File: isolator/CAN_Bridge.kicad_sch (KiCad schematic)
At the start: 45 parts, among them J1 BOOT1, J2 BOOT0, J3 Power in, J4 JTAG5, J5 USART1, J7 HIGHVOLTAGE CAN, J8 LOWVOLTAGE CAN, SW2 SW_Push, U1 STM32F105RBTx, U2 ISO1050DUB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

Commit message: Temp changes
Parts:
- J7, J8: symbol Connector_Generic:Conn_01x02 -> Connector_Generic:Conn_01x04
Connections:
- net +12V: now also J8.2 (Pin_2); no longer J3.1 (Pin_1)
- net +5P: now also J7.2 (Pin_2)
- net GND: now also J8.1 (Pin_1); no longer J3.2 (Pin_2)
- net GND2: now also J7.1 (Pin_1)
- net HV_CANH: now also J7.3 (Pin_3); no longer J7.1 (Pin_1)
- net HV_CANL: now also J7.4 (Pin_4); no longer J7.2 (Pin_2)
- net LV_CANH: now also J8.3 (Pin_3); no longer J8.1 (Pin_1)
- net LV_CANL: now also J8.4 (Pin_4); no longer J8.2 (Pin_2)
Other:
- moved on the sheet: C16, R3, R4

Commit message: Tweaks to schematic
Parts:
- added C7: 10u, Capacitor_SMD:C_0805_2012Metric_Pad1.18x1.45mm_HandSolder, symbol Device:C_Small
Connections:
- net +5P: now also C7.1
- net GND2: now also C7.2
- net LV_RXD: no longer U1.62 (PB9), U5.1 (TXD)
- net LV_TXD: no longer U1.61 (PB8), U5.4 (RXD)
- new net MCU_CAN1_RX: U1.61 (PB8), U5.1 (TXD)
- new net MCU_CAN1_TX: U1.62 (PB9), U5.4 (RXD)
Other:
- note removed: "CAN1_RX"
- company: (none) -> SUFST - Southampton University Formula Student Team
- title: (none) -> TEM Isolator

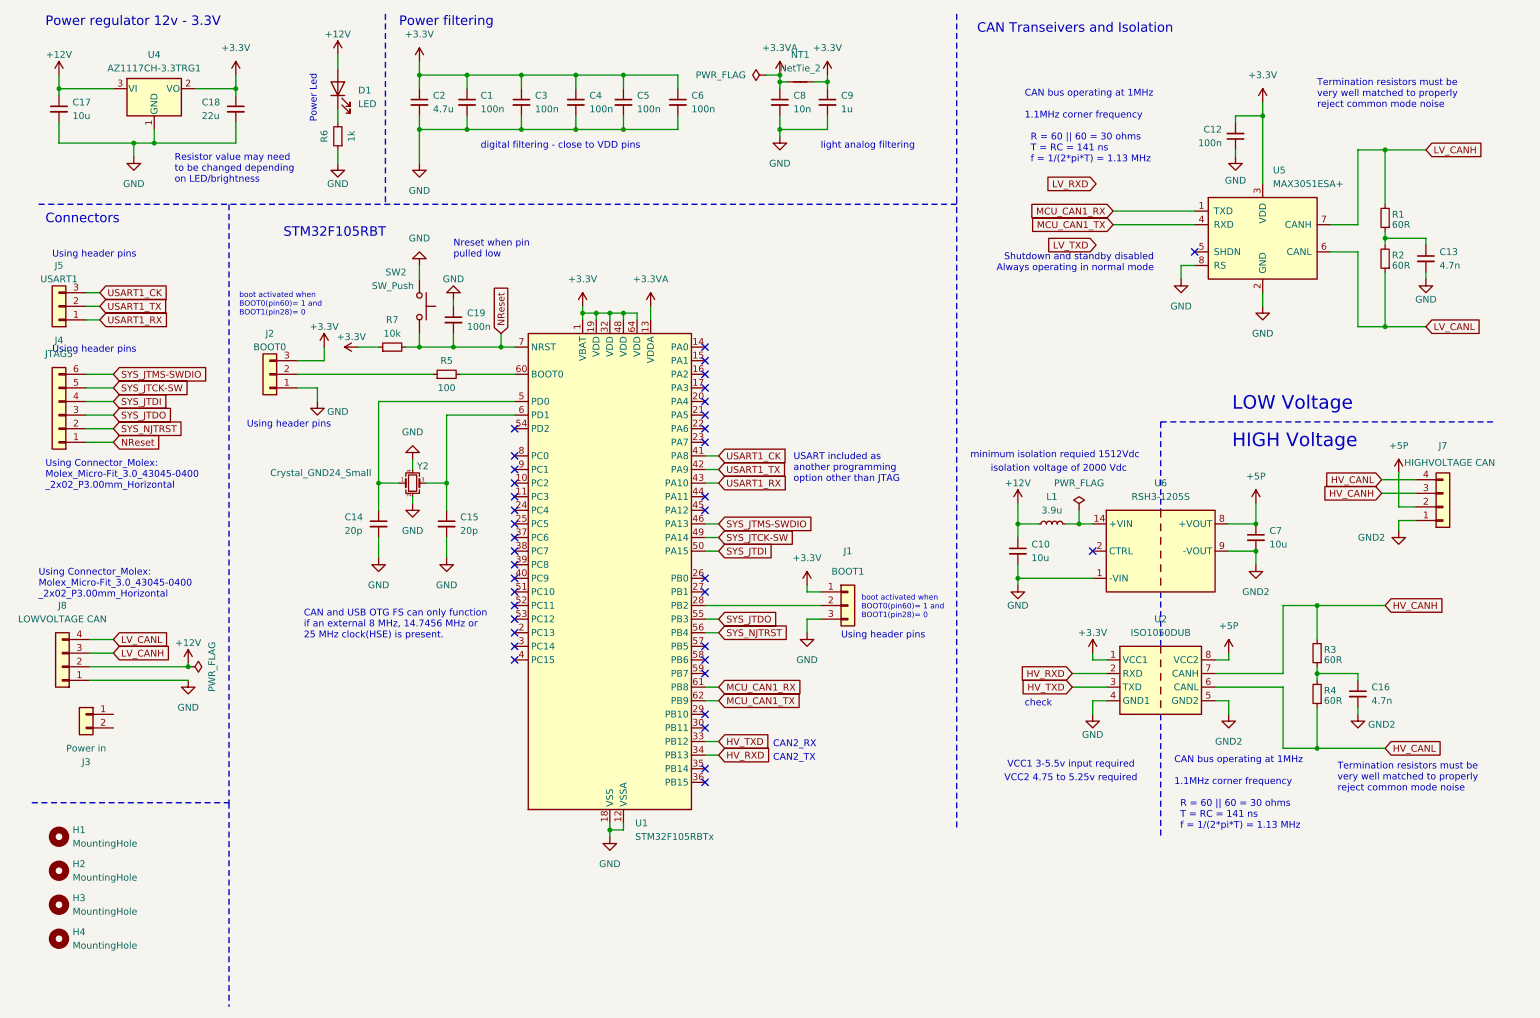
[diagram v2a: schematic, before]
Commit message: Isolator tweaks
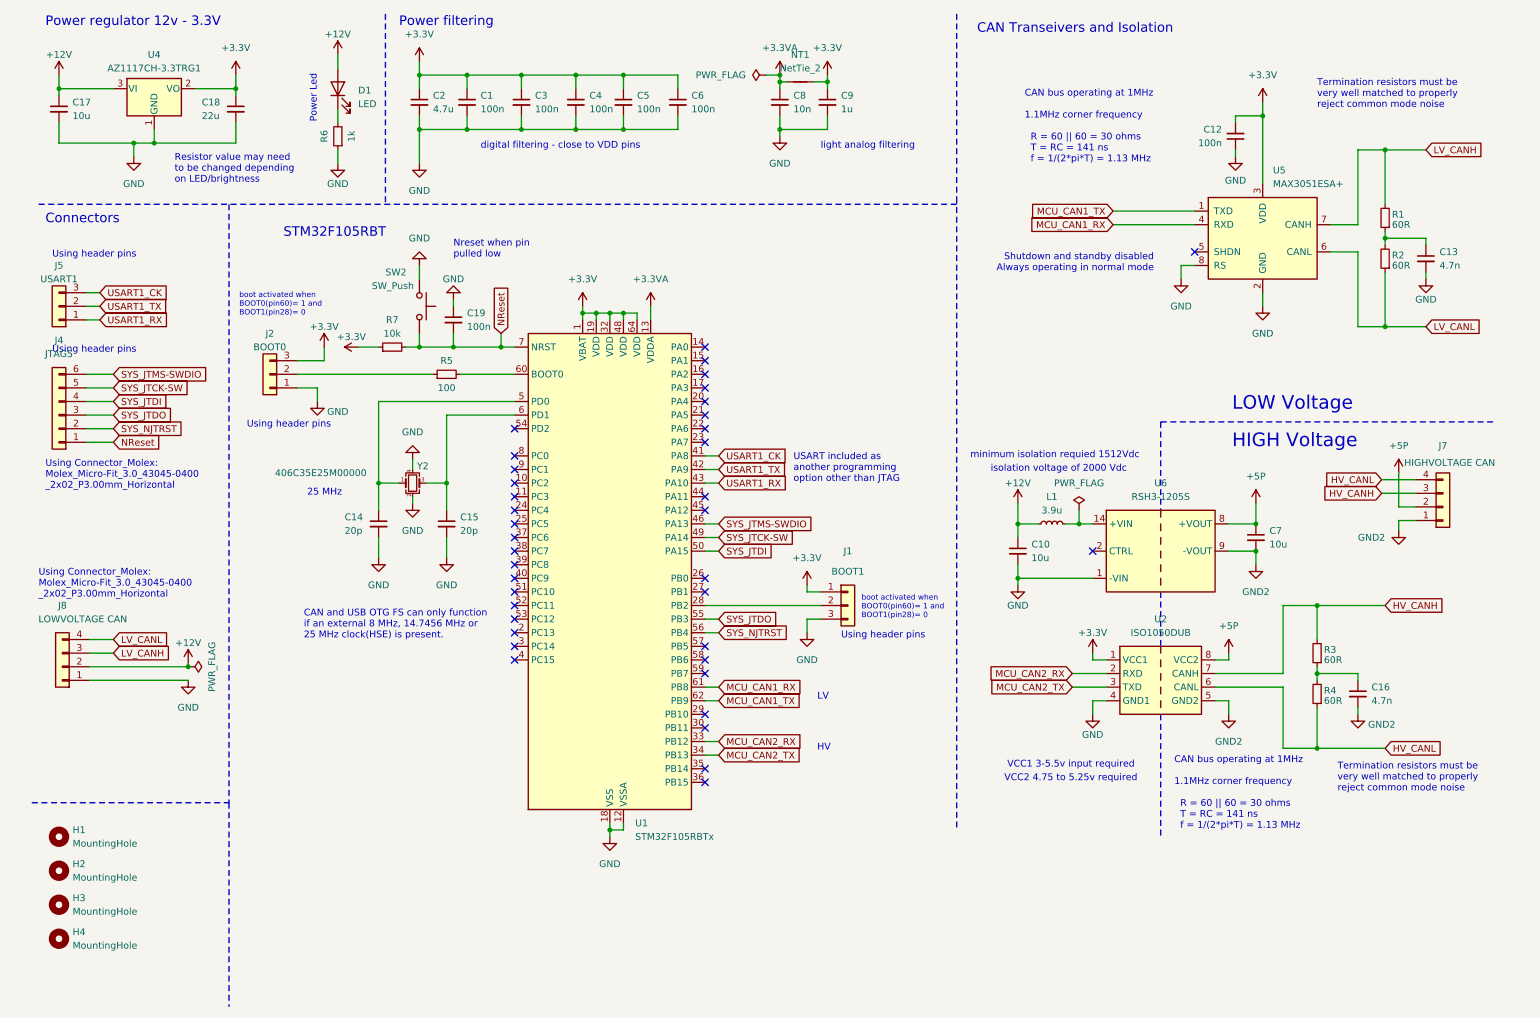
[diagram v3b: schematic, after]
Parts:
- removed J3: Power in, Connector_Molex:Molex_Micro-Fit_3.0_43045-0400_2x02_P3.00mm_Horizontal, symbol Connector_Generic:Conn_01x02
- H1, H2, H3, H4: footprint MountingHole:MountingHole_3mm -> MountingHole:MountingHole_4.3mm_M4
- L1: footprint Capacitor_SMD:C_1206_3216Metric_Pad1.33x1.80mm_HandSolder -> SUFST:RLS-397
- U4: footprint Package_TO_SOT_SMD:SOT-223 -> Package_TO_SOT_SMD:SOT-223-3_TabPin2
- U6: footprint Library:SMDIP-14_15.5mm -> SUFST:SMDIP-14_15.5mm; symbol Converter_DCDC:ATA00A18S-L -> SUFST:RSH3-1205S
- Y2: value Crystal_GND24_Small -> 406C35E25M00000
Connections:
- net MCU_CAN1_RX: now also U5.4 (RXD); no longer U5.1 (TXD)
- net MCU_CAN1_TX: now also U5.1 (TXD); no longer U5.4 (RXD)
- net HV_RXD renamed MCU_CAN2_RX
- net MCU_CAN2_RX: now also U1.33 (PB12); no longer U1.34 (PB13)
- net HV_TXD renamed MCU_CAN2_TX
- net MCU_CAN2_TX: now also U1.34 (PB13); no longer U1.33 (PB12)
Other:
- note added: "25 MHz"
- note added: "HV"
- note added: "LV"
- note removed: "CAN2_RX"
- note removed: "CAN2_TX"
- note removed: "check"

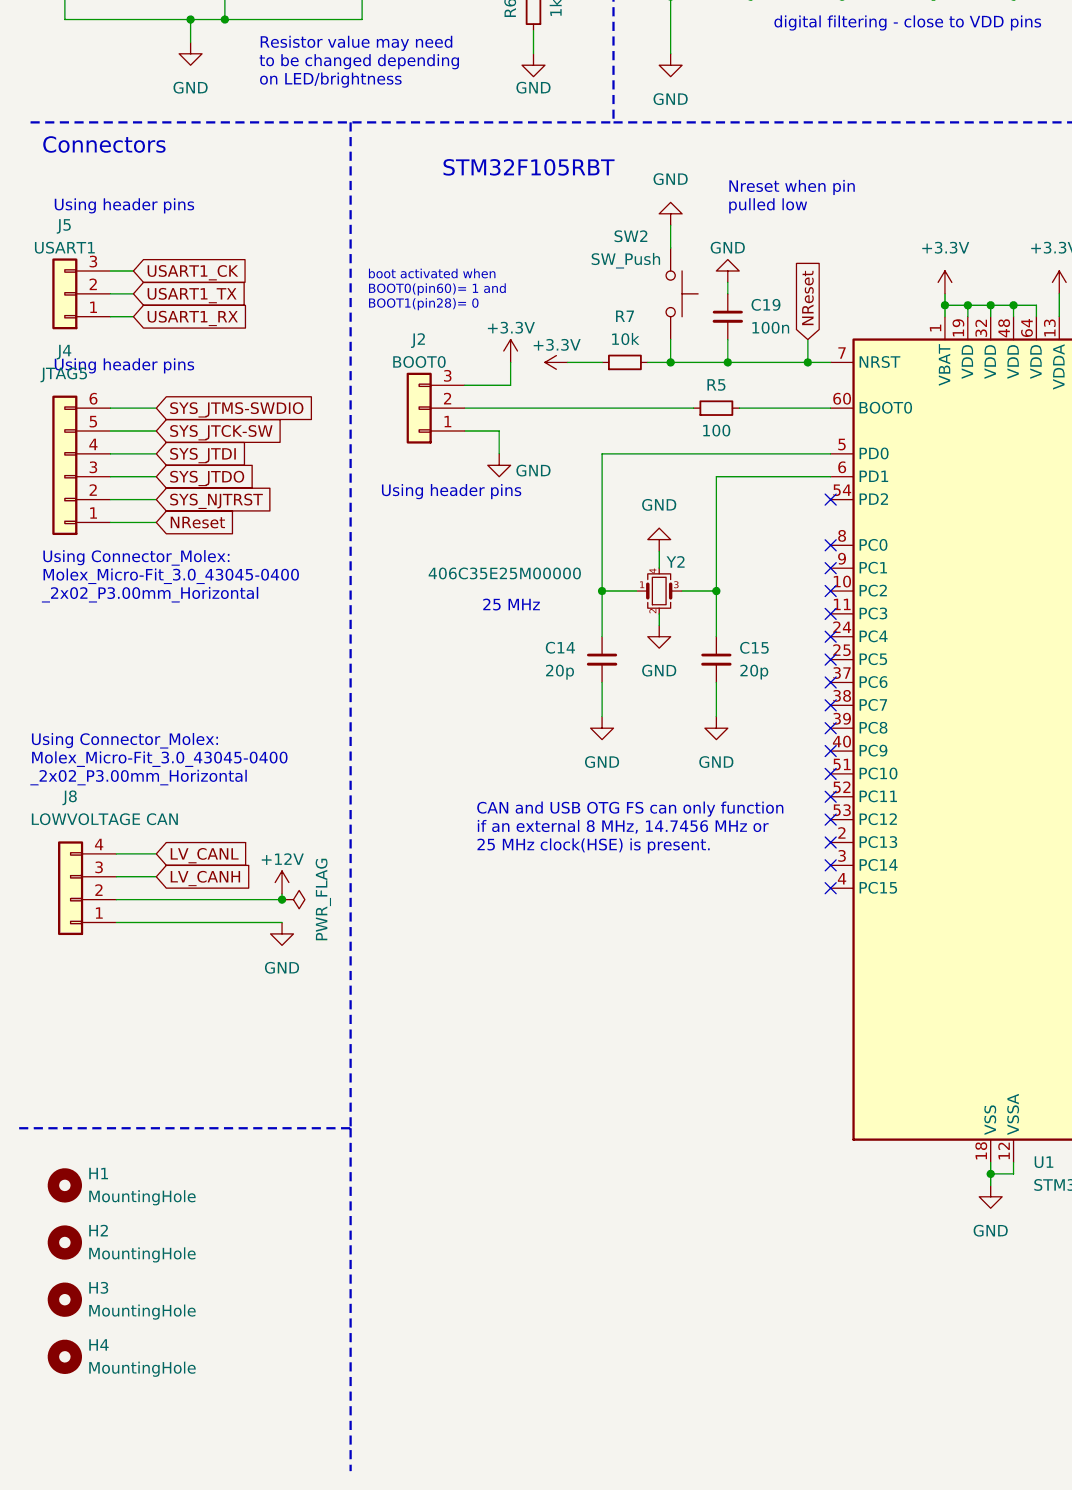
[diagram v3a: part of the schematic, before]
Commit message: Isolator done, pending review
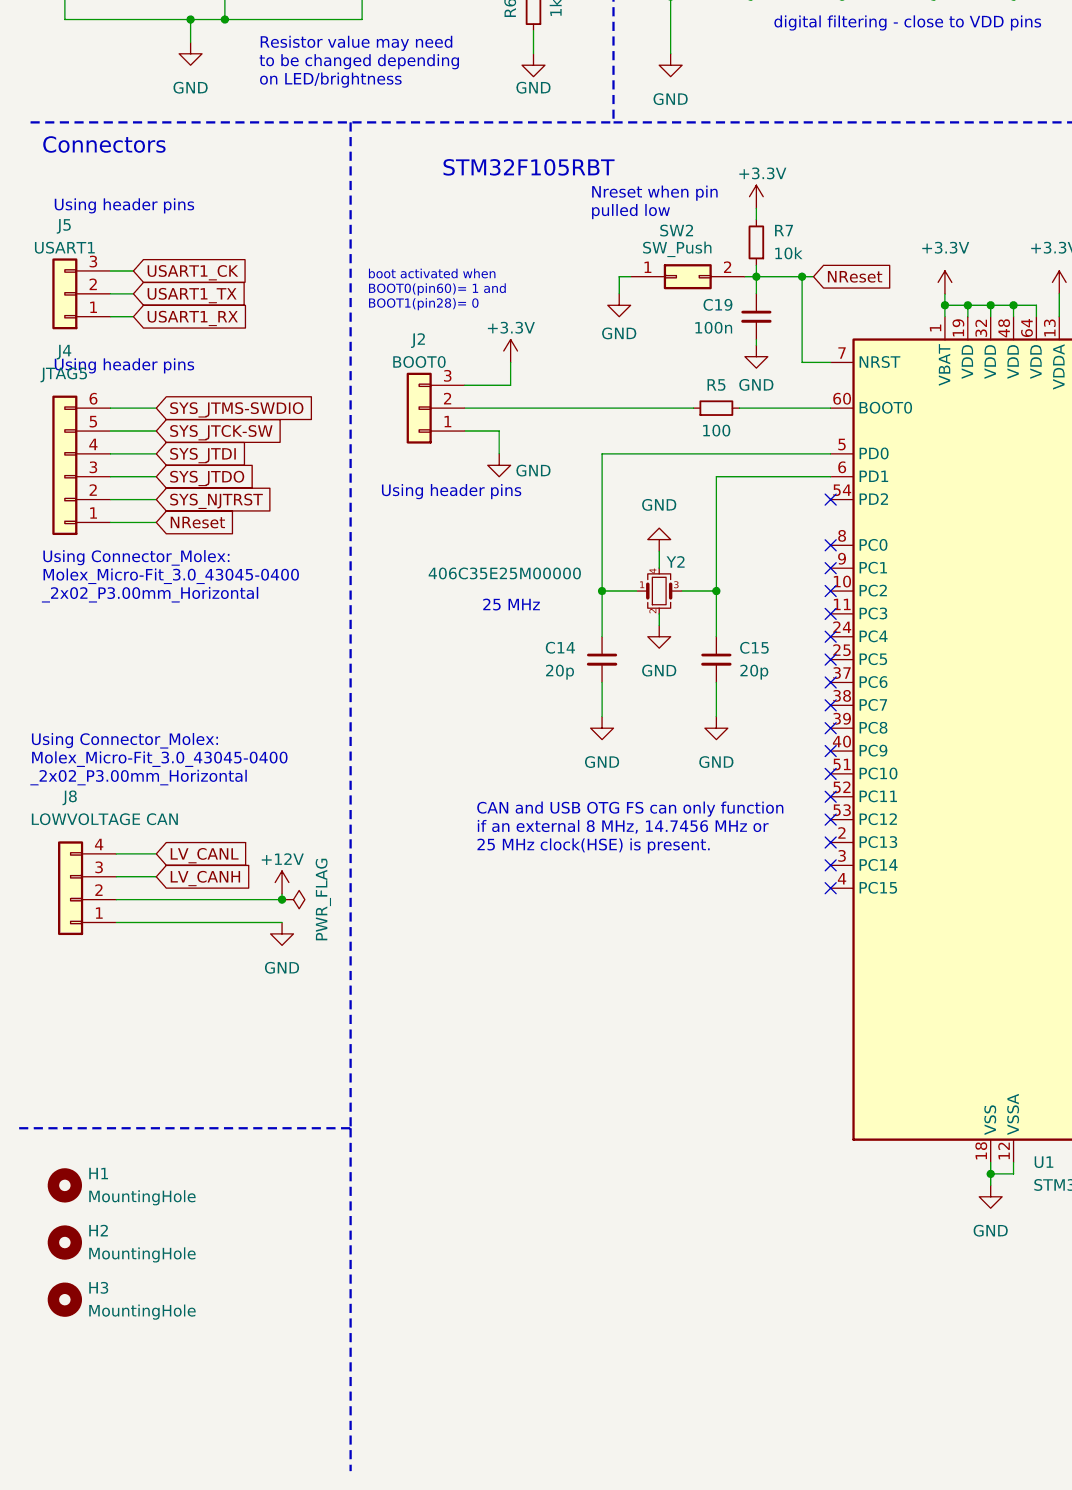
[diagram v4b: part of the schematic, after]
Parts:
- removed H4: MountingHole, MountingHole:MountingHole_4.3mm_M4, symbol Mechanical:MountingHole
- C18: footprint Capacitor_SMD:C_1210_3225Metric_Pad1.33x2.70mm_HandSolder -> Capacitor_SMD:C_1206_3216Metric_Pad1.33x1.80mm_HandSolder
- SW2: footprint Button_Switch_SMD:SW_Push_SPST_NO_Alps_SKRK -> Connector_PinHeader_2.54mm:PinHeader_1x02_P2.54mm_Vertical; symbol Switch:SW_Push -> Connector_Generic:Conn_02x01
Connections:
- net +3.3V: now also R7.2; no longer R7.1
- net GND: now also C19.2; no longer C19.1
- net NReset: now also C19.1, R7.1; no longer C19.2, R7.2
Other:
- moved on the sheet: C19, R7

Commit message: Order codes for BOM
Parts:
- J7, J8: Order Code (none) -> 538-43045-0400
- U1: Order Code (none) -> 511-STM32F105RBT6TR
- U2: Order Code (none) -> 595-ISO1050DUBR
- U4: Order Code (none) -> 621-AZ1117CH-3.3TRG1
- U6: Order Code (none) -> 919-RSH3-1205S/H2
- Y2: Order Code (none) -> 774-406C35E25M00000
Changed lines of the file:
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@@
+      (effects (font (size 1.27 1.27)) hide)
+    )
+    (property "Order Code" "919-RSH3-1205S/H2" (at 222.25 113.03 0)
       (effects (font (size 1.27 1.27)) hide)
     )
@@
     )
     (property "Datasheet" "https://www.st.com/resource/en/datasheet/stm32f105rb.pdf" (at 119.38 118.11 0)
+      (effects (font (size 1.27 1.27)) hide)
+    )
+    (property "Order Code" "511-STM32F105RBT6TR" (at 119.38 118.11 0)
       (effects (font (size 1.27 1.27)) hide)
     )
@@
       (effects (font (size 1.27 1.27)) hide)
     )
+    (property "Order Code" "538-43045-0400" (at 17.145 134.62 0)
+      (effects (font (size 1.27 1.27)) hide)
+    )
     (pin "1")
     (pin "2")
@@
       (effects (font (size 1.27 1.27)) hide)
     )
+    (property "Order Code" "621-AZ1117CH-3.3TRG1" (at 34.29 26.67 0)
+      (effects (font (size 1.27 1.27)) hide)
+    )
     (pin "1")
     (pin "2")
@@
     )
     (property "Datasheet" "http://www.ti.com/lit/ds/symlink/iso1050.pdf" (at 222.25 137.16 0)
+      (effects (font (size 1.27 1.27)) hide)
+    )
+    (property "Order Code" "595-ISO1050DUBR" (at 222.25 135.89 0)
       (effects (font (size 1.27 1.27)) hide)
     )
@@
       (effects (font (size 1.27 1.27)) hide)
     )
+    (property "Order Code" "538-43045-0400" (at 274.955 104.775 0)
+      (effects (font (size 1.27 1.27)) hide)
+    )
     (pin "1")
     (pin "2")
@@
       (effects (font (size 1.27 1.27)) hide)
     )
+    (property "Order Code" "774-406C35E25M00000" (at 82.55 100.33 0)
+      (effects (font (size 1.27 1.27)) hide)
+    )
